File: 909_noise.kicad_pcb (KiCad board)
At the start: 2 copper layers, 0 parts

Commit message: initial placement, schematic tweaks
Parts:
- added C1: 100n, Capacitor_SMD:C_0603_1608Metric, F.Cu at (60.2, 22.5)
- added C2: 4.7u, Capacitor_SMD:C_0805_2012Metric, F.Cu at (55.0, 24.5)
- added C3: 100n, Capacitor_SMD:C_0603_1608Metric, F.Cu at (56.5, 27.5)
- added C4: 100n, Capacitor_SMD:C_0603_1608Metric, F.Cu at (67.0, 22.0)
- added C5: 330n, Capacitor_SMD:C_0603_1608Metric, F.Cu at (51.2, 24.5)
- added D1: green, LED_SMD:LED_0603_1608Metric, F.Cu at (47.0, 37.8)
- added J1: Conn_01x02_Pin, Connector_PinHeader_2.54mm:PinHeader_1x02_P2.54mm_Vertical, F.Cu at (47.0, 28.7)
- added J2: Conn_01x03_Pin, Connector_PinHeader_2.54mm:PinHeader_1x03_P2.54mm_Vertical, F.Cu at (72.5, 27.5)
- added J3: Conn_ARM_JTAG_SWD_10, Connector_PinHeader_1.27mm:PinHeader_2x05_P1.27mm_Vertical_SMD, F.Cu at (65.7, 36.3)
- added R1: 10k, Resistor_SMD:R_0603_1608Metric, F.Cu at (47.0, 34.8)
- added R2: 10k, Resistor_SMD:R_0603_1608Metric, F.Cu at (65.5, 29.5)
- added R3: 10k, Resistor_SMD:R_0603_1608Metric, F.Cu at (67.0, 29.5)
- added SW1: PTS645SM43SMTR92 LFS, Button_Switch_SMD:SW_SPST_PTS645, F.Cu at (54.0, 36.2)
- added U1: STM32G030J6Mx, Package_SO:SOIC-8_3.9x4.9mm_P1.27mm, F.Cu at (61.0, 28.0)
- added U2: L78L33ABUTR, Package_TO_SOT_SMD:SOT-89-3, F.Cu at (52.5, 29.5)
- added U3: TLV7211A, Package_TO_SOT_SMD:SOT-23-5, F.Cu at (66.5, 25.5)
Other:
- board outline added: 30 x 20 mm

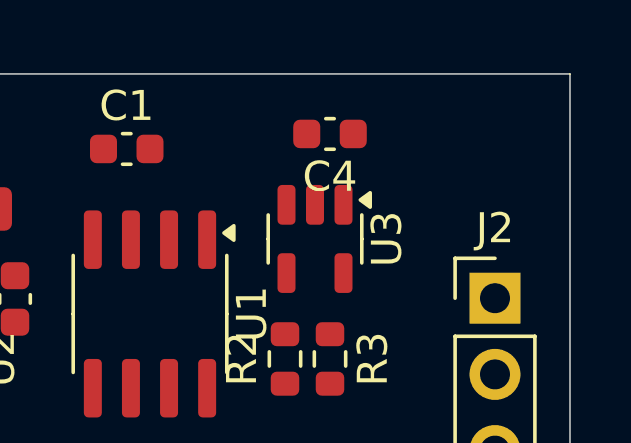
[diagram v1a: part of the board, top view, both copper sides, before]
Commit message: add output filter
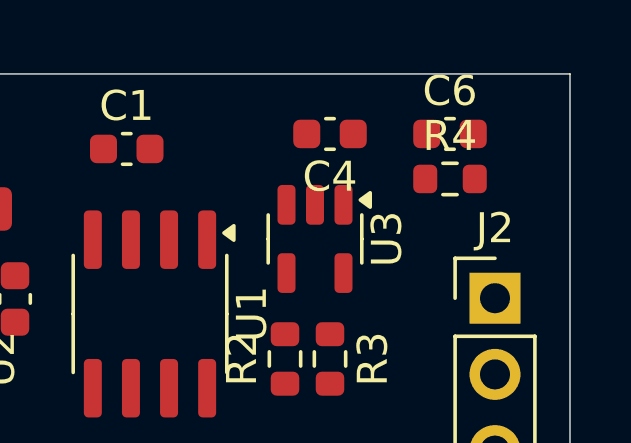
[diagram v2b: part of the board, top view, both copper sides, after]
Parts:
- added C6: 100n, Capacitor_SMD:C_0603_1608Metric, F.Cu at (71.0, 22.0)
- added R4: 15, Resistor_SMD:R_0603_1608Metric, F.Cu at (71.0, 23.5)
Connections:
- J2 pad 2: /noise_12v -> /noise_12v_filtered

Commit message: quick silk adjust
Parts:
- moved D1 0.44 mm to (46.6, 38.0)
- moved R1 0.44 mm to (46.6, 35.0)
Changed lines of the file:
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@@
 		(tags "capacitor")
 		(property "Reference" "C6"
-			(at 0 -1.43 0)
+			(at 2.6 0 0)
 			(layer "F.SilkS")
 			(effects
@@
 		(tags "SPST Button Switch")
 		(property "Reference" "SW1"
-			(at 0 -4.05 180)
+			(at -5.82 -1.95 -90)
 			(layer "F.SilkS")
 			(effects
@@
 		(tags "capacitor")
 		(property "Reference" "C5"
-			(at 0 -1.43 180)
+			(at 0.225 1.7 180)
 			(layer "F.SilkS")
 			(effects
@@
 	(footprint "Resistor_SMD:R_0603_1608Metric"
 		(layer "F.Cu")
-		(at 47 34.825 90)
+		(at 46.6 35 90)
 		(descr "Resistor SMD 0603 (1608 Metric), square (rectangular) end terminal, IPC_7351 nominal, (Body size source: IPC-SM-782 page 72, https://www.pcb-3d.com/wordpress/wp-content/uploads/ipc-sm-782a_amendment_1_and_2.pdf), generated with kicad-footprint-generator")
 		(tags "resistor")
 		(property "Reference" "R1"
-			(at 0 -1.43 270)
+			(at 0 1.6 270)
 			(layer "F.SilkS")
 			(effects
@@
 		(tags "resistor")
 		(property "Reference" "R2"
-			(at 0 -1.43 270)
+			(at -2.5 -0.3 0)
 			(layer "F.SilkS")
 			(effects
@@
 		(tags "Surface mounted pin header SMD 2x05 1.27mm double row")
 		(property "Reference" "J3"
-			(at 0 -4.235 270)
+			(at -2.53 -4.13 270)
 			(layer "F.SilkS")
 			(effects
@@
 		(tags "SOIC SO")
 		(property "Reference" "U1"
-			(at 0 -3.4 90)
+			(at -4.6 -2.2 180)
 			(layer "F.SilkS")
 			(effects
@@
 		(tags "capacitor")
 		(property "Reference" "C4"
-			(at 0 -1.43 180)
+			(at 2.6 0 180)
 			(layer "F.SilkS")
 			(effects
@@
 		(tags "resistor")
 		(property "Reference" "R4"
-			(at 0 -1.43 0)
+			(at 2.6 0.1 0)
 			(layer "F.SilkS")
 			(effects
@@
 		(tags "SOT-89-3")
 		(property "Reference" "U2"
-			(at 0 -3.5 90)
+			(at 1.1 -3.3 90)
 			(layer "F.SilkS")
 			(effects
@@
 		(tags "resistor")
 		(property "Reference" "R3"
-			(at 0 -1.43 90)
+			(at 2.5 -0.4 180)
 			(layer "F.SilkS")
 			(effects
@@
 	(footprint "LED_SMD:LED_0603_1608Metric"
 		(layer "F.Cu")
-		(at 47 37.825 -90)
+		(at 46.6 38 -90)
 		(descr "LED SMD 0603 (1608 Metric), square (rectangular) end terminal, IPC_7351 nominal, (Body size source: http://www.tortai-tech.com/upload/download/2011102023233369053.pdf), generated with kicad-footprint-generator")
 		(tags "LED")
 		(property "Reference" "D1"
-			(at 0 -1.43 90)
+			(at 0 -1.6 90)
 			(layer "F.SilkS")
 			(effects
@@
 		(tags "capacitor")
 		(property "Reference" "C3"
-			(at 0 -1.43 270)
+			(at -3.1 0.9 270)
 			(layer "F.SilkS")
 			(effects

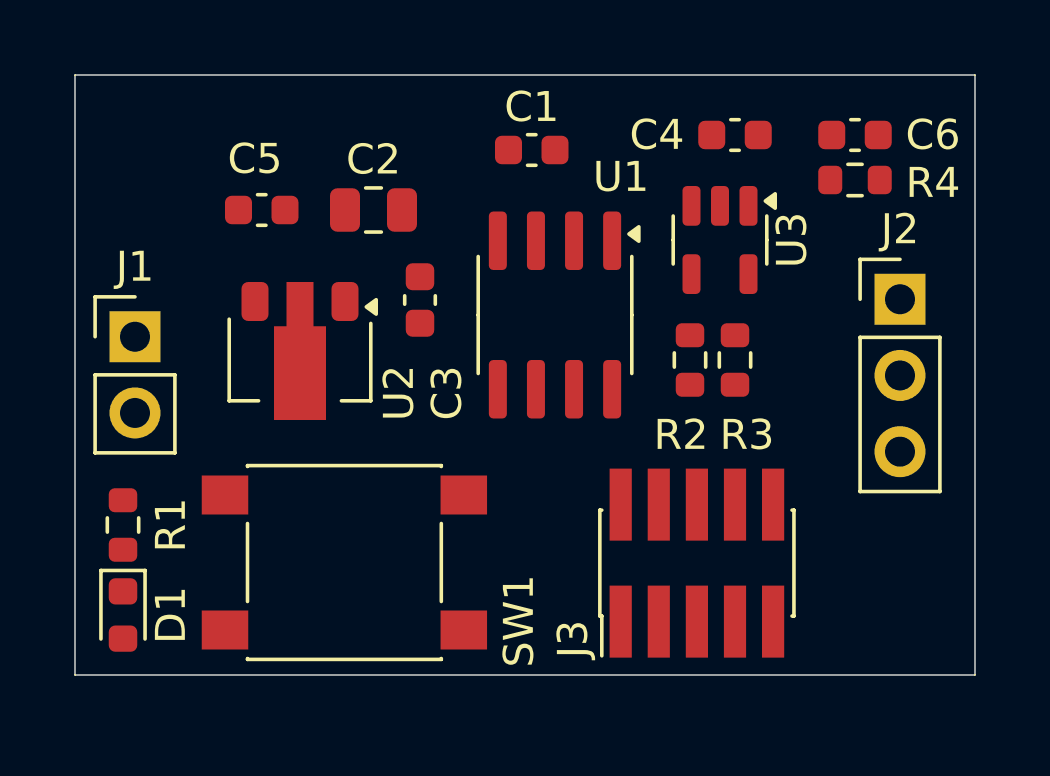
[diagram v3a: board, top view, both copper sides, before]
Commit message: add netclasses and a gnd fill
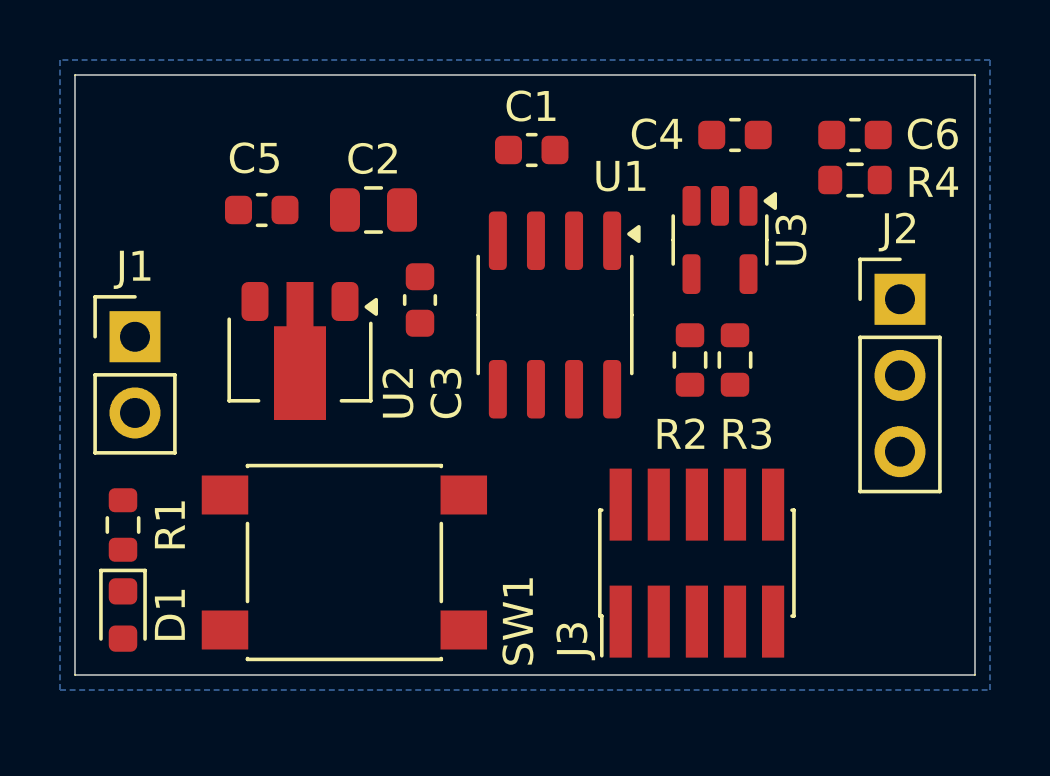
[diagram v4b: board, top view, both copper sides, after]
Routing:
- added copper zone on B.Cu, net GND
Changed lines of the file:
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@@
 			(extension_offset 0.5) keep_text_aligned)
 	)
+	(zone
+		(net 1)
+		(net_name "GND")
+		(layer "B.Cu")
+		(hatch edge 0.5)
+		(connect_pads
+			(clearance 0.5)
+		)
+		(min_thickness 0.25)
+		(filled_areas_thickness no)
+		(fill yes
+			(thermal_gap 0.5)
+			(thermal_bridge_width 0.5)
+		)
+		(polygon
+			(pts
+				(xy 44.5 19.5) (xy 44.5 40.5) (xy 75.5 40.5) (xy 75.5 19.5)
+			)
+		)
+	)
 )

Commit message: initial layout
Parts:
- moved R2 5.06 mm to (64.8, 24.5), turned to -90 degrees
- moved R3 3.01 mm to (64.8, 27.5)
- moved C1 1.08 mm to (61.0, 23.2)
- moved C4 1.06 mm to (67.8, 22.8)
- moved U3 0.79 mm to (67.2, 25.8)
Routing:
- net +3.3V: track 0.00 -> 47.7 mm
- net /~{reset}: track 0.00 -> 33.9 mm
- net +12V: track 0.00 -> 28.5 mm
- net GND: track 0.00 -> 27.2 mm, vias 0 -> 15
- net Net-(D1-A): track 0.00 -> 18.5 mm
- net /noise_12v_filtered: track 0.00 -> 9.34 mm
- net /swdio: track 0.00 -> 4.49 mm
- net /swclk: track 0.00 -> 4.49 mm
- net /noise_3v3: track 0.00 -> 3.87 mm
- net Net-(U3--): track 0.00 -> 2.99 mm
- net /noise_12v: track 0.00 -> 2.44 mm
- net Net-(D1-K): track 0.00 -> 1.39 mm

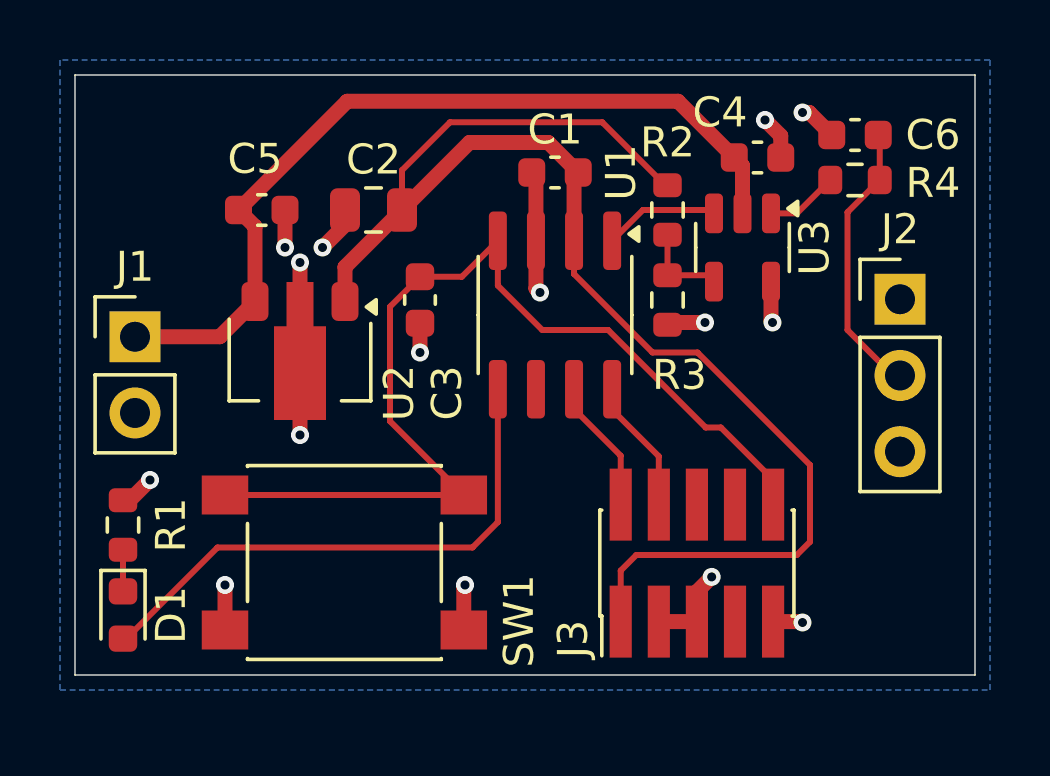
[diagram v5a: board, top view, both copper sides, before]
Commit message: fillet board outline
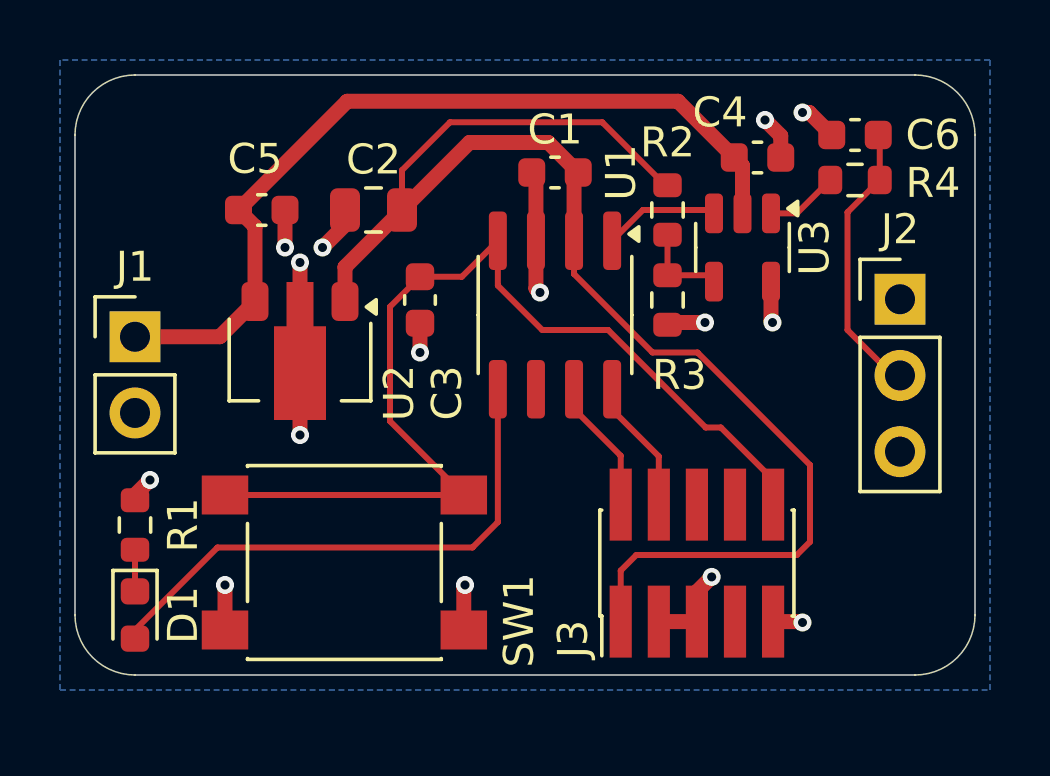
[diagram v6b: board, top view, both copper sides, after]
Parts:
- moved D1 0.40 mm to (47.0, 38.0)
- moved R1 0.40 mm to (47.0, 35.0)
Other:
- outline, holes or cut-outs redrawn
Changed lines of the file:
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@@
 	(footprint "Resistor_SMD:R_0603_1608Metric"
 		(layer "F.Cu")
-		(at 46.6 35 90)
+		(at 47 35 90)
 		(descr "Resistor SMD 0603 (1608 Metric), square (rectangular) end terminal, IPC_7351 nominal, (Body size source: IPC-SM-782 page 72, https://www.pcb-3d.com/wordpress/wp-content/uploads/ipc-sm-782a_amendment_1_and_2.pdf), generated with kicad-footprint-generator")
 		(tags "resistor")
@@
 	(footprint "LED_SMD:LED_0603_1608Metric"
 		(layer "F.Cu")
-		(at 46.6 38 -90)
+		(at 47 38 -90)
 		(descr "LED SMD 0603 (1608 Metric), square (rectangular) end terminal, IPC_7351 nominal, (Body size source: http://www.tortai-tech.com/upload/download/2011102023233369053.pdf), generated with kicad-footprint-generator")
 		(tags "LED")
@@
 		)
 	)
-	(gr_rect
-		(start 45 20)
-		(end 75 40)
+	(gr_arc
+		(start 45 22)
+		(mid 45.585786 20.585786)
+		(end 47 20)
+		(stroke
+			(width 0.05)
+			(type default)
+		)
+		(layer "Edge.Cuts")
+	)
+	(gr_line
+		(start 45 38)
+		(end 45 22)
+		(stroke
+			(width 0.05)
+			(type default)
+		)
+		(layer "Edge.Cuts")
+	)
+	(gr_line
+		(start 73 40)
+		(end 47 40)
+		(stroke
+			(width 0.05)
+			(type default)
+		)
+		(layer "Edge.Cuts")
+	)
+	(gr_arc
+		(start 73 20)
+		(mid 74.414214 20.585786)
+		(end 75 22)
+		(stroke
+			(width 0.05)
+			(type default)
+		)
+		(layer "Edge.Cuts")
+	)
+	(gr_arc
+		(start 47 40)
+		(mid 45.585786 39.414214)
+		(end 45 38)
+		(stroke
+			(width 0.05)
+			(type default)
+		)
+		(layer "Edge.Cuts")
+	)
+	(gr_line
+		(start 47 20)
+		(end 73 20)
+		(stroke
+			(width 0.05)
+			(type default)
+		)
+		(layer "Edge.Cuts")
+	)
+	(gr_arc
+		(start 75 38)
+		(mid 74.414214 39.414214)
+		(end 73 40)
+		(stroke
+			(width 0.05)
+			(type default)
+		)
+		(layer "Edge.Cuts")
+	)
+	(gr_line
+		(start 75 22)
+		(end 75 38)
 		(stroke
 			(width 0.05)
 			(type default)
 		)
-		(fill none)
 		(layer "Edge.Cuts")
 	)
@@
 	)
 	(segment
+		(start 47 34.175)
+		(end 47 34)
+		(width 0.5)
+		(layer "F.Cu")
+		(net 1)
+	)
+	(segment
 		(start 54 24.5)
 		(end 54 25)
@@
 	)
 	(segment
-		(start 46.6 34.175)
-		(end 46.825 34.175)
-		(width 0.5)
-		(layer "F.Cu")
-		(net 1)
-	)
-	(segment
 		(start 60.365 25.525)
 		(end 60.365 27.115)
@@
 	)
 	(segment
-		(start 46.825 34.175)
-		(end 47.5 33.5)
-		(width 0.5)
-		(layer "F.Cu")
-		(net 1)
-	)
-	(segment
 		(start 64.46 38.22)
 		(end 65.73 38.22)
@@
 		(net 1)
 	)
+	(segment
+		(start 47 34)
+		(end 47.5 33.5)
+		(width 0.5)
+		(layer "F.Cu")
+		(net 1)
+	)
 	(via
 		(at 68.25 28.25)
@@
 	)
 	(segment
-		(start 46.6 35.825)
-		(end 46.6 37.2125)
+		(start 47 35.825)
+		(end 47 37.2125)
 		(width 0.2)
 		(layer "F.Cu")
@@
 	)
 	(segment
-		(start 49.75 35.75)
-		(end 58.25 35.75)
+		(start 59.095 34.905)
+		(end 59.095 30.475)
 		(width 0.2)
 		(layer "F.Cu")
@@
 	)
 	(segment
-		(start 59.095 34.905)
-		(end 59.095 30.475)
+		(start 47 38.7875)
+		(end 47 38.5)
 		(width 0.2)
 		(layer "F.Cu")
@@
 	)
 	(segment
-		(start 46.7125 38.7875)
-		(end 49.75 35.75)
+		(start 49.75 35.75)
+		(end 58.25 35.75)
 		(width 0.2)
 		(layer "F.Cu")
@@
 	)
 	(segment
-		(start 46.6 38.7875)
-		(end 46.7125 38.7875)
+		(start 47 38.5)
+		(end 49.75 35.75)
 		(width 0.2)
 		(layer "F.Cu")

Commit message: flip connectors to bottom
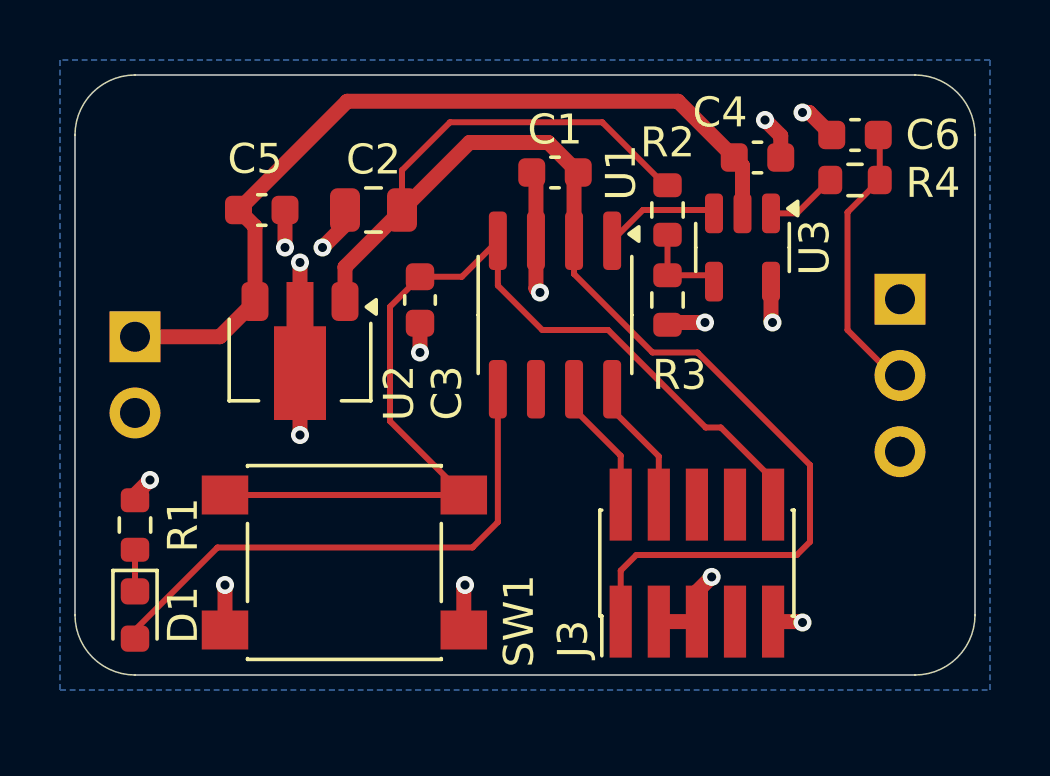
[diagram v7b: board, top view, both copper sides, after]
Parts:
- J1, J2: moved to B.Cu
- turned J1 to 180 degrees
- turned J2 to 180 degrees

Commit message: adjust connector position and add connector dims
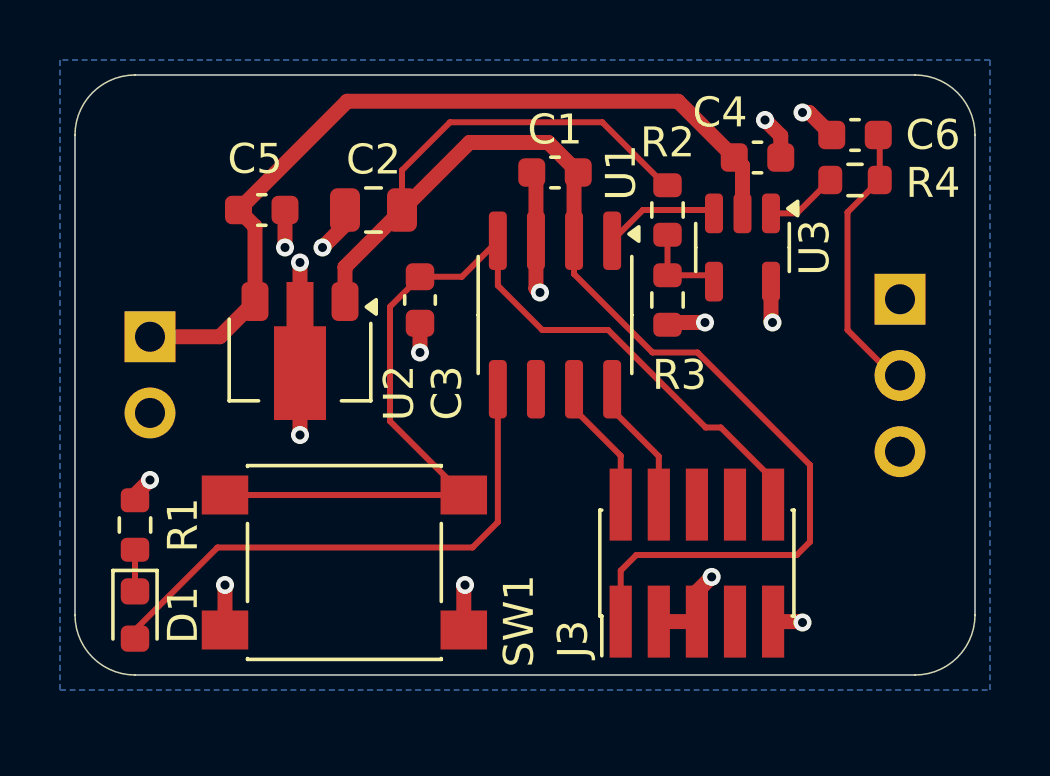
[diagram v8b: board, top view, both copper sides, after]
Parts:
- moved J1 0.50 mm to (47.5, 28.7)
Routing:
- net +12V: track 28.5 -> 28.0 mm
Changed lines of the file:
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@@
 			(at -0.775 0)
 			(size 0.9 0.95)
-			(layers "F.Cu" "F.Paste" "F.Mask")
+			(layers "F.Cu")
 			(roundrect_rratio 0.25)
 			(net 1 "GND")
@@
 			(at 0.775 0)
 			(size 0.9 0.95)
-			(layers "F.Cu" "F.Paste" "F.Mask")
+			(layers "F.Cu")
 			(roundrect_rratio 0.25)
 			(net 16 "/noise_12v_filtered")
@@
 			(at 0.825 0)
 			(size 0.8 0.95)
-			(layers "F.Cu" "F.Paste" "F.Mask")
+			(layers "F.Cu")
 			(roundrect_rratio 0.25)
 			(net 16 "/noise_12v_filtered")
@@
 	(footprint "Connector_PinHeader_2.54mm:PinHeader_1x02_P2.54mm_Vertical"
 		(layer "B.Cu")
-		(at 47 28.725 180)
+		(at 47.5 28.725 180)
 		(descr "Through hole straight pin header, 1x02, 2.54mm pitch, single row")
 		(tags "Through hole pin header THT 1x02 2.54mm single row")
@@
 			(extension_offset 0.5) keep_text_aligned)
 	)
+	(dimension
+		(type orthogonal)
+		(layer "Dwgs.User")
+		(pts
+			(xy 72.5 27.475) (xy 47.5 28.725)
+		)
+		(height -9.975)
+		(orientation 0)
+		(gr_text "25.0000 mm"
+			(at 60 16.35 0)
+			(layer "Dwgs.User")
+			(effects
+				(font
+					(size 1 1)
+					(thickness 0.15)
+				)
+			)
+		)
+		(format
+			(prefix "")
+			(suffix "")
+			(units 3)
+			(units_format 1)
+			(precision 4)
+		)
+		(style
+			(thickness 0.1)
+			(arrow_length 1.27)
+			(text_position_mode 0)
+			(extension_height 0.58642)
+			(extension_offset 0.5) keep_text_aligned)
+	)
+	(dimension
+		(type orthogonal)
+		(layer "Dwgs.User")
+		(pts
+			(xy 72.5 30) (xy 73 20)
+		)
+		(height 7.5)
+		(orientation 1)
+		(gr_text "10.0000 mm"
+			(at 78.85 25 90)
+			(layer "Dwgs.User")
+			(effects
+				(font
+					(size 1 1)
+					(thickness 0.15)
+				)
+			)
+		)
+		(format
+			(prefix "")
+			(suffix "")
+			(units 3)
+			(units_format 1)
+			(precision 4)
+		)
+		(style
+			(thickness 0.1)
+			(arrow_length 1.27)
+			(text_position_mode 0)
+			(extension_height 0.58642)
+			(extension_offset 0.5) keep_text_aligned)
+	)
 	(segment
 		(start 54 25)
@@
 	)
 	(segment
-		(start 47 28.725)
+		(start 47.5 28.725)
 		(end 49.825 28.725)
 		(width 0.5)
@@
 	)
 	(segment
+		(start 49.825 28.725)
+		(end 51 27.55)
+		(width 0.5)
+		(layer "F.Cu")
+		(net 4)
+	)
+	(segment
 		(start 66.975 22.75)
 		(end 67.25 23.025)
@@
 		(width 0.5)
 		(layer "F.Cu")
-		(net 4)
-	)
-	(segment
-		(start 49.825 28.725)
-		(end 51 27.55)
-		(width 0.5)
-		(layer "F.Cu")
